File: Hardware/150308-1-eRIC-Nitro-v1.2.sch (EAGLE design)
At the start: 39 parts, among them IC1 ATmega328P-AU, IC2 MIC5205-3.3, K1 M12PTH, K2 M12PTH, K4 FTDI Basic, K6 SMA_EDGE, X1 8MHz

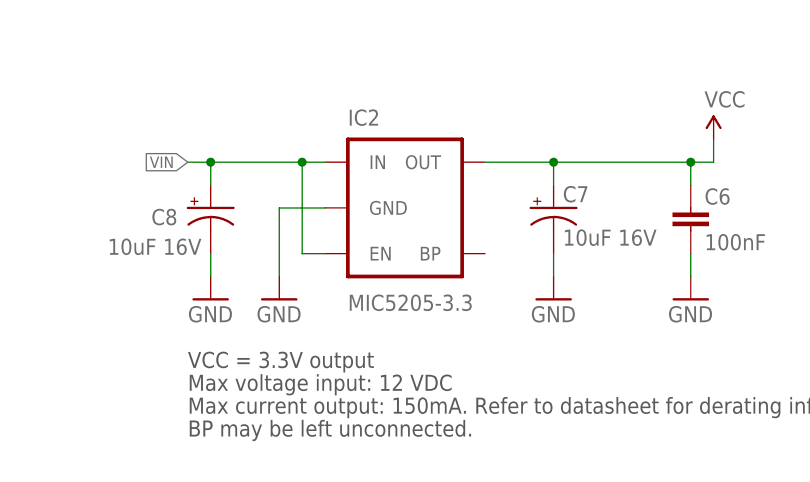
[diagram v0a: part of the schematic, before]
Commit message: Small cosmetic changes, new bootloader
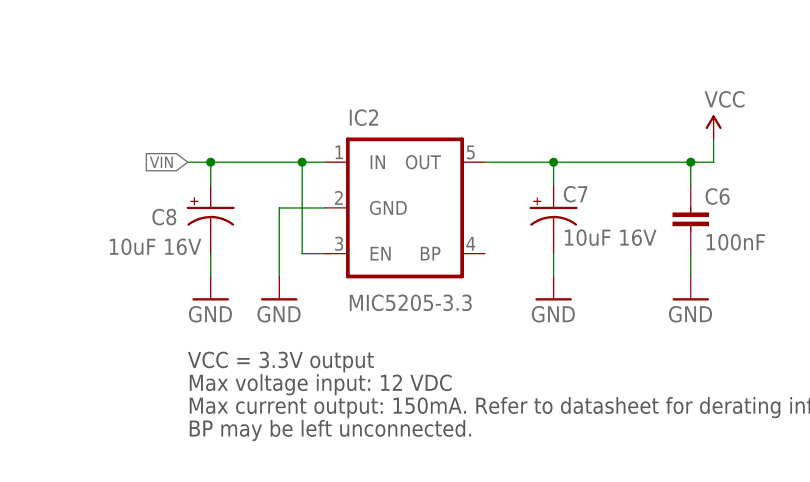
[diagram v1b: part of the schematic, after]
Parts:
- IC2: device SparkFun:V_REG_LDOSMD -> 150308-1-eRIC-Nitro:V_REG_LDOSMD
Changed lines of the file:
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@@
 <?xml version="1.0" encoding="utf-8"?>
 <!DOCTYPE eagle SYSTEM "eagle.dtd">
-<eagle version="6.5.0">
+<eagle version="7.3.0">
 <drawing>
 <settings>
@@
 <part name="LED1" library="150308-1-eRIC-Nitro" deviceset="LED" device="" value="Green"/>
 <part name="GND8" library="SparkFun" deviceset="GND" device=""/>
-<part name="IC2" library="SparkFun" deviceset="V_REG_LDO" device="SMD" value="MIC5205-3.3"/>
+<part name="IC2" library="150308-1-eRIC-Nitro" deviceset="V_REG_LDO" device="SMD" value="MIC5205-3.3"/>
 <part name="C8" library="150308-1-eRIC-Nitro" deviceset="CAP_POL" device="1206" value="10uF 16V"/>
 <part name="GND30" library="SparkFun" deviceset="GND" device=""/>
